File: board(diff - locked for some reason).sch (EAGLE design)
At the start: 18 parts, among them IC1 ATMEGA644-20PU, Q1 2N3906, T1 2N3904, T2 2N3904, T3 2N3904, T4 2N3904

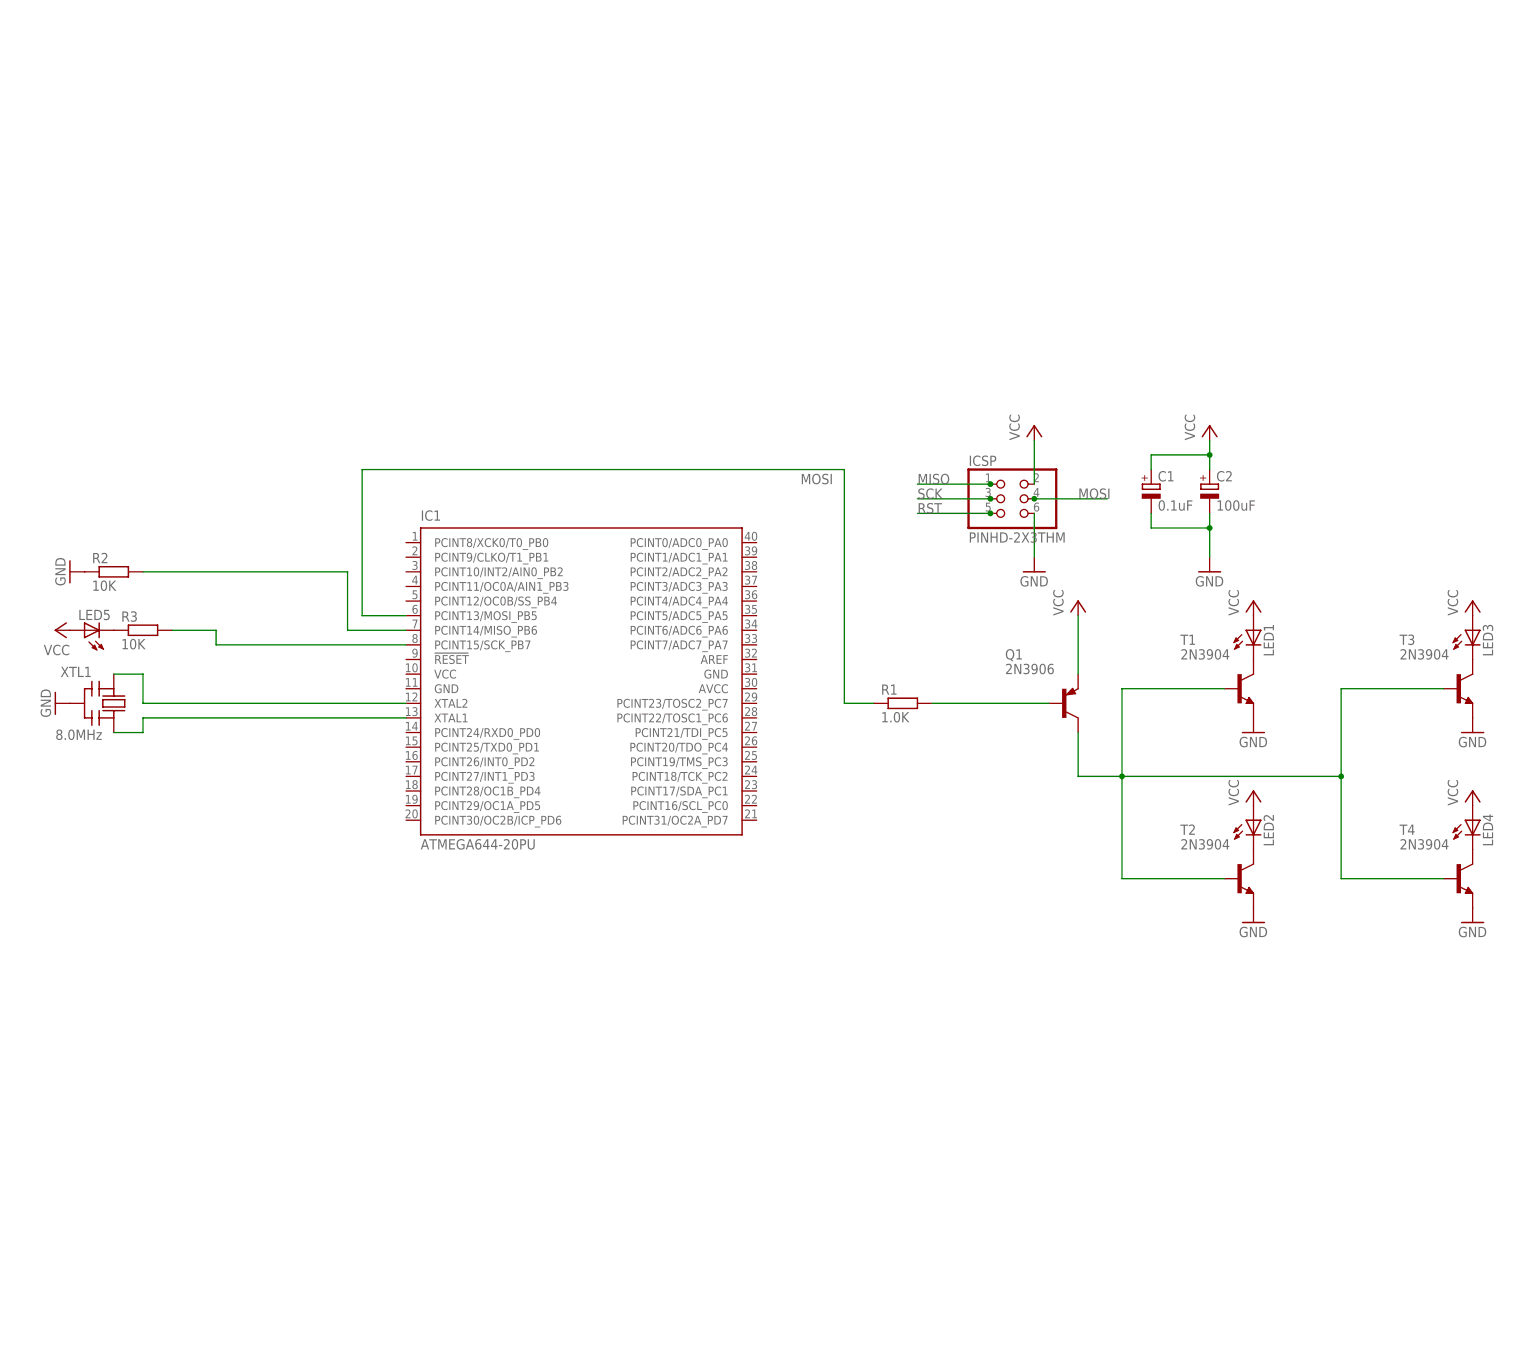
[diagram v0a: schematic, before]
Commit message: modified design and added ada library
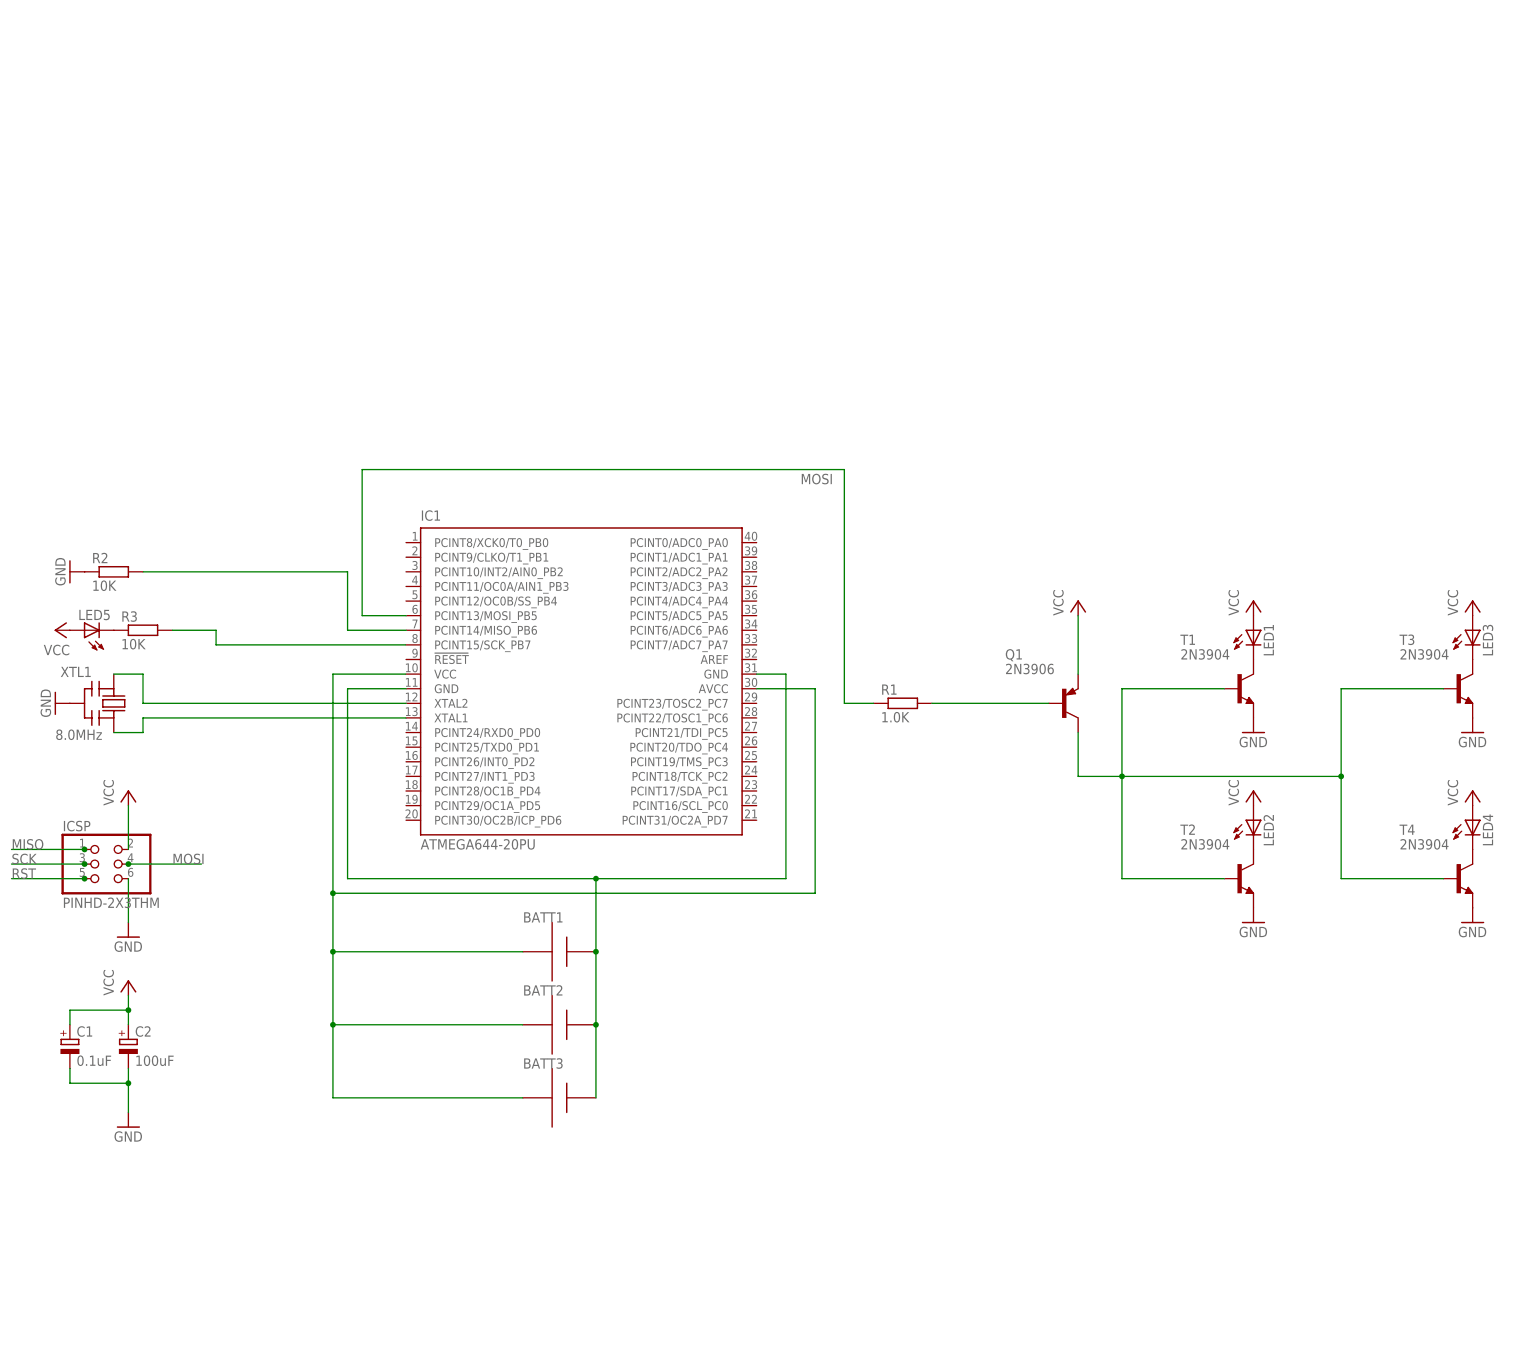
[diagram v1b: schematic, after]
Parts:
- added BATT1, BATT2, BATT3: AAA, adafruit:AAA
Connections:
- new net N$12: BATT1.+, BATT2.+, BATT3.+, IC1.GND, IC1.GND@1
- new net N$14: BATT1.-, BATT2.-, BATT3.-, IC1.AVCC, IC1.VCC
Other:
- moved on the sheet: C1, C2, ICSP

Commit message: modified board some more
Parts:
- removed BATT1, BATT2, BATT3: AAA, adafruit:AAA
- removed LED1, LED2, LED4: (no value), led:LED3MM
- added LED6, LED8, LED9: LED, tvbgone:LED
- added U1: MCP1825S-3302E/DB, MCP1825S-3302E_DB:MCP1825S-3302E/DB
- LED3: value (none) -> LED; device led:LED3MM -> tvbgone:LED
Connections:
- new net N$13: IC1.!RESET
- net N$1: now also LED6.C, LED6.C1; no longer LED1.C
- net N$12: no longer BATT1.+, BATT2.+, BATT3.+
- net N$14: no longer BATT1.-, BATT2.-, BATT3.-
- net N$2: now also LED3.C1
- net N$3: now also LED8.C, LED8.C1; no longer LED2.C
- net N$4: now also LED9.C, LED9.C1; no longer LED4.C
- net VCC: now also LED3.A1, LED6.A, LED6.A1, LED8.A, LED8.A1, LED9.A, LED9.A1; no longer LED1.A, LED2.A, LED4.A
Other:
- moved on the sheet: T2, T4

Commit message: modified board slightly
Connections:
- net GND: now also U1.GND_(TAB), U1.GND_(TAB)_2
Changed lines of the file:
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@@
 <?xml version="1.0" encoding="utf-8"?>
 <!DOCTYPE eagle SYSTEM "eagle.dtd">
-<eagle version="8.4.0">
+<eagle version="8.4.1">
 <drawing>
 <settings>
@@
 <part name="P+4" library="supply1" library_urn="urn:adsk.eagle:library:371" deviceset="VCC" device=""/>
 <part name="U1" library="MCP1825S-3302E_DB" deviceset="MCP1825S-3302E/DB" device=""/>
+<part name="GND8" library="supply1" library_urn="urn:adsk.eagle:library:371" deviceset="GND" device=""/>
 </parts>
 <sheets>
@@
 <instance part="P+4" gate="VCC" x="93.98" y="71.12"/>
 <instance part="U1" gate="A" x="-81.28" y="33.02"/>
+<instance part="GND8" gate="1" x="-111.76" y="17.78"/>
 </instances>
 <busses>
@@
 <junction x="-139.7" y="20.32"/>
 </segment>
+<segment>
+<pinref part="U1" gate="A" pin="GND_(TAB)"/>
+<wire x1="-104.14" y1="27.94" x2="-111.76" y2="27.94" width="0.1524" layer="91"/>
+<wire x1="-111.76" y1="27.94" x2="-111.76" y2="25.4" width="0.1524" layer="91"/>
+<pinref part="U1" gate="A" pin="GND_(TAB)_2"/>
+<wire x1="-111.76" y1="25.4" x2="-111.76" y2="20.32" width="0.1524" layer="91"/>
+<wire x1="-104.14" y1="25.4" x2="-111.76" y2="25.4" width="0.1524" layer="91"/>
+<junction x="-111.76" y="25.4"/>
+<pinref part="GND8" gate="1" pin="GND"/>
+</segment>
 </net>

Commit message: added battery holders
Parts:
- added J1, J2, J3: 2468, SamacSys_Parts:2468
- added JP1, JP2: (no value), pinhead:PINHD-2X4
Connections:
- new net N$16: J1.POS, J2.POS, J3.POS, U1.VIN
- net GND: now also J1.NEG, J2.NEG, J3.NEG
- net N$14: now also U1.VOUT
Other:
- moved on the sheet: U1
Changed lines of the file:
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@@
 <?xml version="1.0" encoding="utf-8"?>
 <!DOCTYPE eagle SYSTEM "eagle.dtd">
-<eagle version="8.4.1">
+<eagle version="8.3.1">
 <drawing>
 <settings>
@@
 <part name="U1" library="MCP1825S-3302E_DB" deviceset="MCP1825S-3302E/DB" device=""/>
 <part name="GND8" library="supply1" library_urn="urn:adsk.eagle:library:371" deviceset="GND" device=""/>
+<part name="JP1" library="pinhead" library_urn="urn:adsk.eagle:library:325" deviceset="PINHD-2X4" device="" package3d_urn="urn:adsk.eagle:package:22461/2"/>
+<part name="JP2" library="pinhead" library_urn="urn:adsk.eagle:library:325" deviceset="PINHD-2X4" device="" package3d_urn="urn:adsk.eagle:package:22461/2"/>
+<part name="J1" library="SamacSys_Parts" deviceset="2468" device=""/>
+<part name="J2" library="SamacSys_Parts" deviceset="2468" device=""/>
+<part name="J3" library="SamacSys_Parts" deviceset="2468" device=""/>
+<part name="GND9" library="supply1" library_urn="urn:adsk.eagle:library:371" deviceset="GND" device=""/>
 </parts>
 <sheets>
@@
 <instance part="P+3" gate="VCC" x="55.88" y="71.12"/>
 <instance part="P+4" gate="VCC" x="93.98" y="71.12"/>
-<instance part="U1" gate="A" x="-81.28" y="33.02"/>
-<instance part="GND8" gate="1" x="-111.76" y="17.78"/>
+<instance part="U1" gate="A" x="-76.2" y="17.78" rot="R90"/>
+<instance part="GND8" gate="1" x="-68.58" y="-22.86"/>
+<instance part="JP1" gate="A" x="7.62" y="68.58"/>
+<instance part="JP2" gate="A" x="7.62" y="50.8"/>
+<instance part="J1" gate="G$1" x="-40.64" y="38.1"/>
+<instance part="J2" gate="G$1" x="-40.64" y="25.4"/>
+<instance part="J3" gate="G$1" x="-40.64" y="12.7"/>
+<instance part="GND9" gate="1" x="-10.16" y="5.08"/>
 </instances>
 <busses>
@@
 </segment>
 <segment>
+<wire x1="-68.58" y1="-15.24" x2="-68.58" y2="-20.32" width="0.1524" layer="91"/>
+<pinref part="GND8" gate="1" pin="GND"/>
 <pinref part="U1" gate="A" pin="GND_(TAB)"/>
-<wire x1="-104.14" y1="27.94" x2="-111.76" y2="27.94" width="0.1524" layer="91"/>
-<wire x1="-111.76" y1="27.94" x2="-111.76" y2="25.4" width="0.1524" layer="91"/>
+<wire x1="-71.12" y1="-5.08" x2="-71.12" y2="-15.24" width="0.1524" layer="91"/>
+<wire x1="-71.12" y1="-15.24" x2="-68.58" y2="-15.24" width="0.1524" layer="91"/>
 <pinref part="U1" gate="A" pin="GND_(TAB)_2"/>
-<wire x1="-111.76" y1="25.4" x2="-111.76" y2="20.32" width="0.1524" layer="91"/>
-<wire x1="-104.14" y1="25.4" x2="-111.76" y2="25.4" width="0.1524" layer="91"/>
-<junction x="-111.76" y="25.4"/>
-<pinref part="GND8" gate="1" pin="GND"/>
+<wire x1="-68.58" y1="-15.24" x2="-68.58" y2="-5.08" width="0.1524" layer="91"/>
+<junction x="-68.58" y="-15.24"/>
+</segment>
+<segment>
+<pinref part="J1" gate="G$1" pin="NEG"/>
+<wire x1="-15.24" y1="38.1" x2="-10.16" y2="38.1" width="0.1524" layer="91"/>
+<wire x1="-10.16" y1="38.1" x2="-10.16" y2="25.4" width="0.1524" layer="91"/>
+<pinref part="J3" gate="G$1" pin="NEG"/>
+<wire x1="-10.16" y1="25.4" x2="-10.16" y2="12.7" width="0.1524" layer="91"/>
+<wire x1="-10.16" y1="12.7" x2="-15.24" y2="12.7" width="0.1524" layer="91"/>
+<pinref part="J2" gate="G$1" pin="NEG"/>
+<wire x1="-15.24" y1="25.4" x2="-10.16" y2="25.4" width="0.1524" layer="91"/>
+<junction x="-10.16" y="25.4"/>
+<wire x1="-10.16" y1="12.7" x2="-10.16" y2="7.62" width="0.1524" layer="91"/>
+<junction x="-10.16" y="12.7"/>
+<pinref part="GND9" gate="1" pin="GND"/>
 </segment>
 </net>
@@
 <wire x1="-20.32" y1="88.9" x2="-20.32" y2="53.34" width="0.1524" layer="91"/>
 <wire x1="-20.32" y1="53.34" x2="-104.14" y2="53.34" width="0.1524" layer="91"/>
+<pinref part="U1" gate="A" pin="VOUT"/>
+<wire x1="-71.12" y1="40.64" x2="-104.14" y2="40.64" width="0.1524" layer="91"/>
+<wire x1="-104.14" y1="40.64" x2="-104.14" y2="53.34" width="0.1524" layer="91"/>
+<junction x="-104.14" y="53.34"/>
 </segment>
 </net>
@@
 </segment>
 </net>
+<net name="N$16" class="0">
+<segment>
+<pinref part="J1" gate="G$1" pin="POS"/>
+<pinref part="J2" gate="G$1" pin="POS"/>
+<wire x1="-40.64" y1="38.1" x2="-40.64" y2="25.4" width="0.1524" layer="91"/>
+<pinref part="J3" gate="G$1" pin="POS"/>
+<wire x1="-40.64" y1="12.7" x2="-40.64" y2="25.4" width="0.1524" layer="91"/>
+<junction x="-40.64" y="25.4"/>
+<wire x1="-40.64" y1="12.7" x2="-40.64" y2="-10.16" width="0.1524" layer="91"/>
+<junction x="-40.64" y="12.7"/>
+<wire x1="-40.64" y1="-10.16" x2="-76.2" y2="-10.16" width="0.1524" layer="91"/>
+<pinref part="U1" gate="A" pin="VIN"/>
+<wire x1="-76.2" y1="-10.16" x2="-76.2" y2="-5.08" width="0.1524" layer="91"/>
+</segment>
+</net>
